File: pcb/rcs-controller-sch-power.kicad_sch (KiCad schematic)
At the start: 62 parts, among them J1 00222-32051, J10 0022-232021, J2 0022-232021, J3 0022-232041, J8 00222-32051, Q1 SI7465DP-T1-E3, U2 MP26123DR-LF-Z, U3 TPS63070

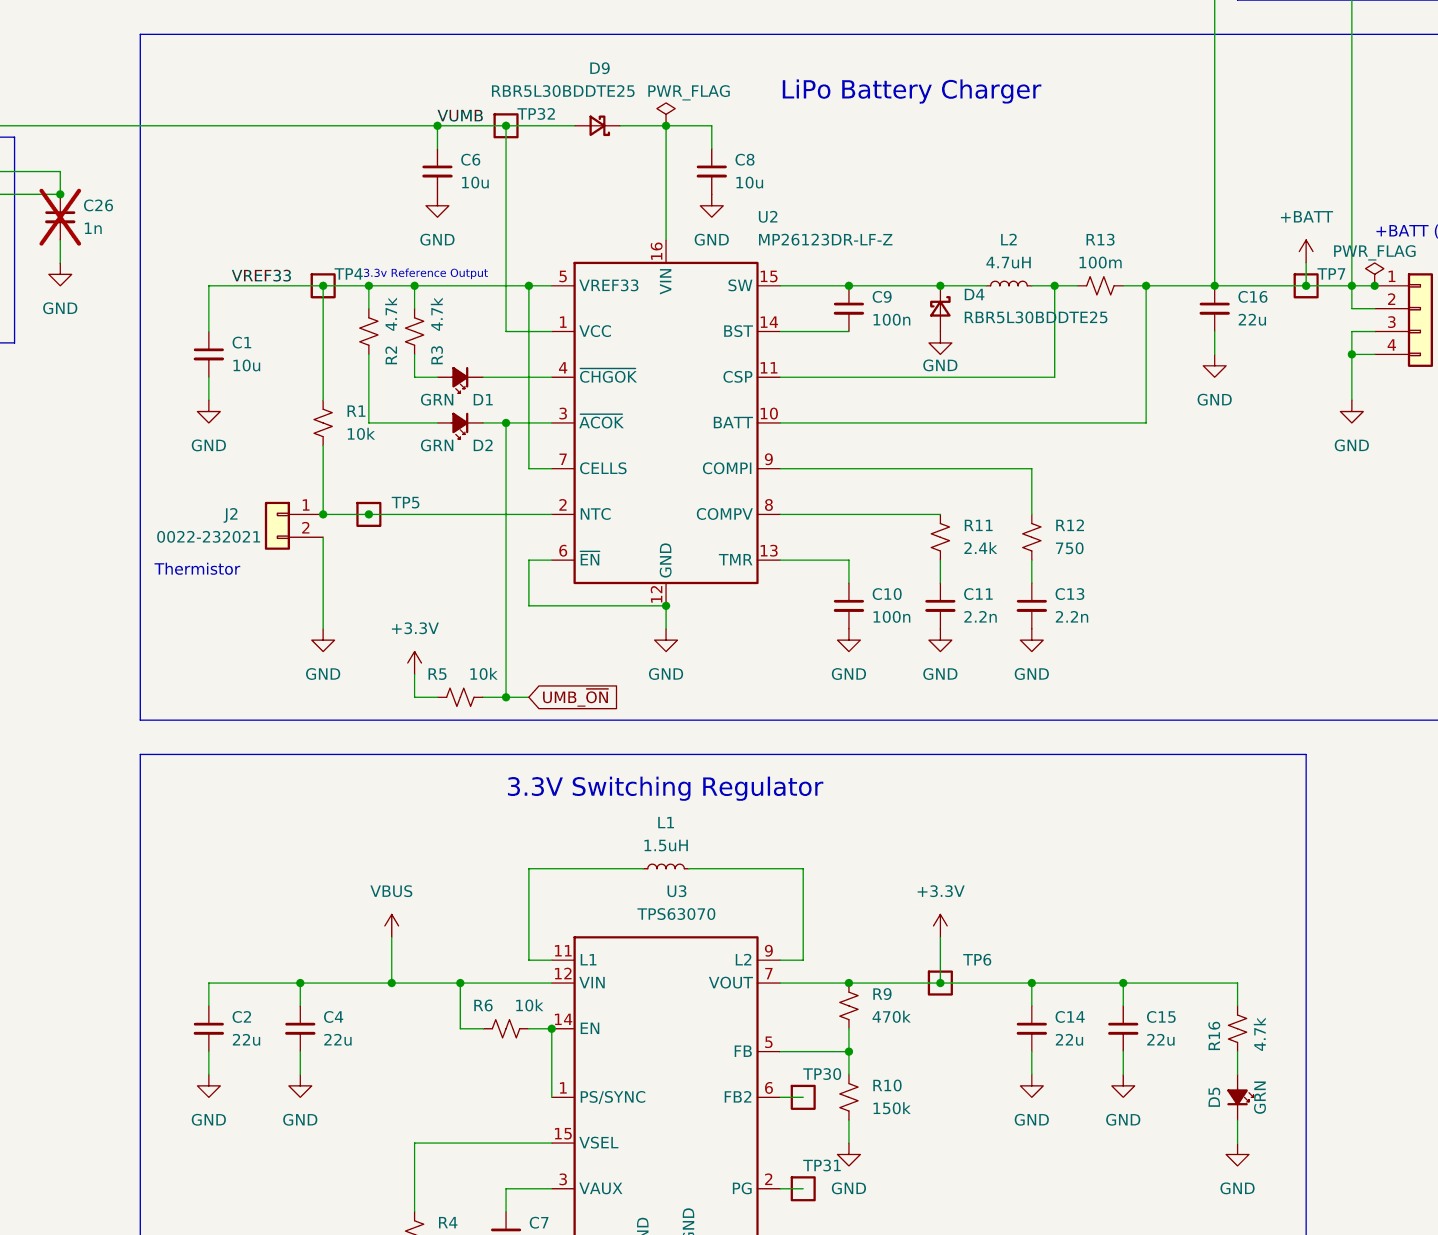
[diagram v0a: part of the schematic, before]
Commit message: power OR cleanup with Thomas for USB power
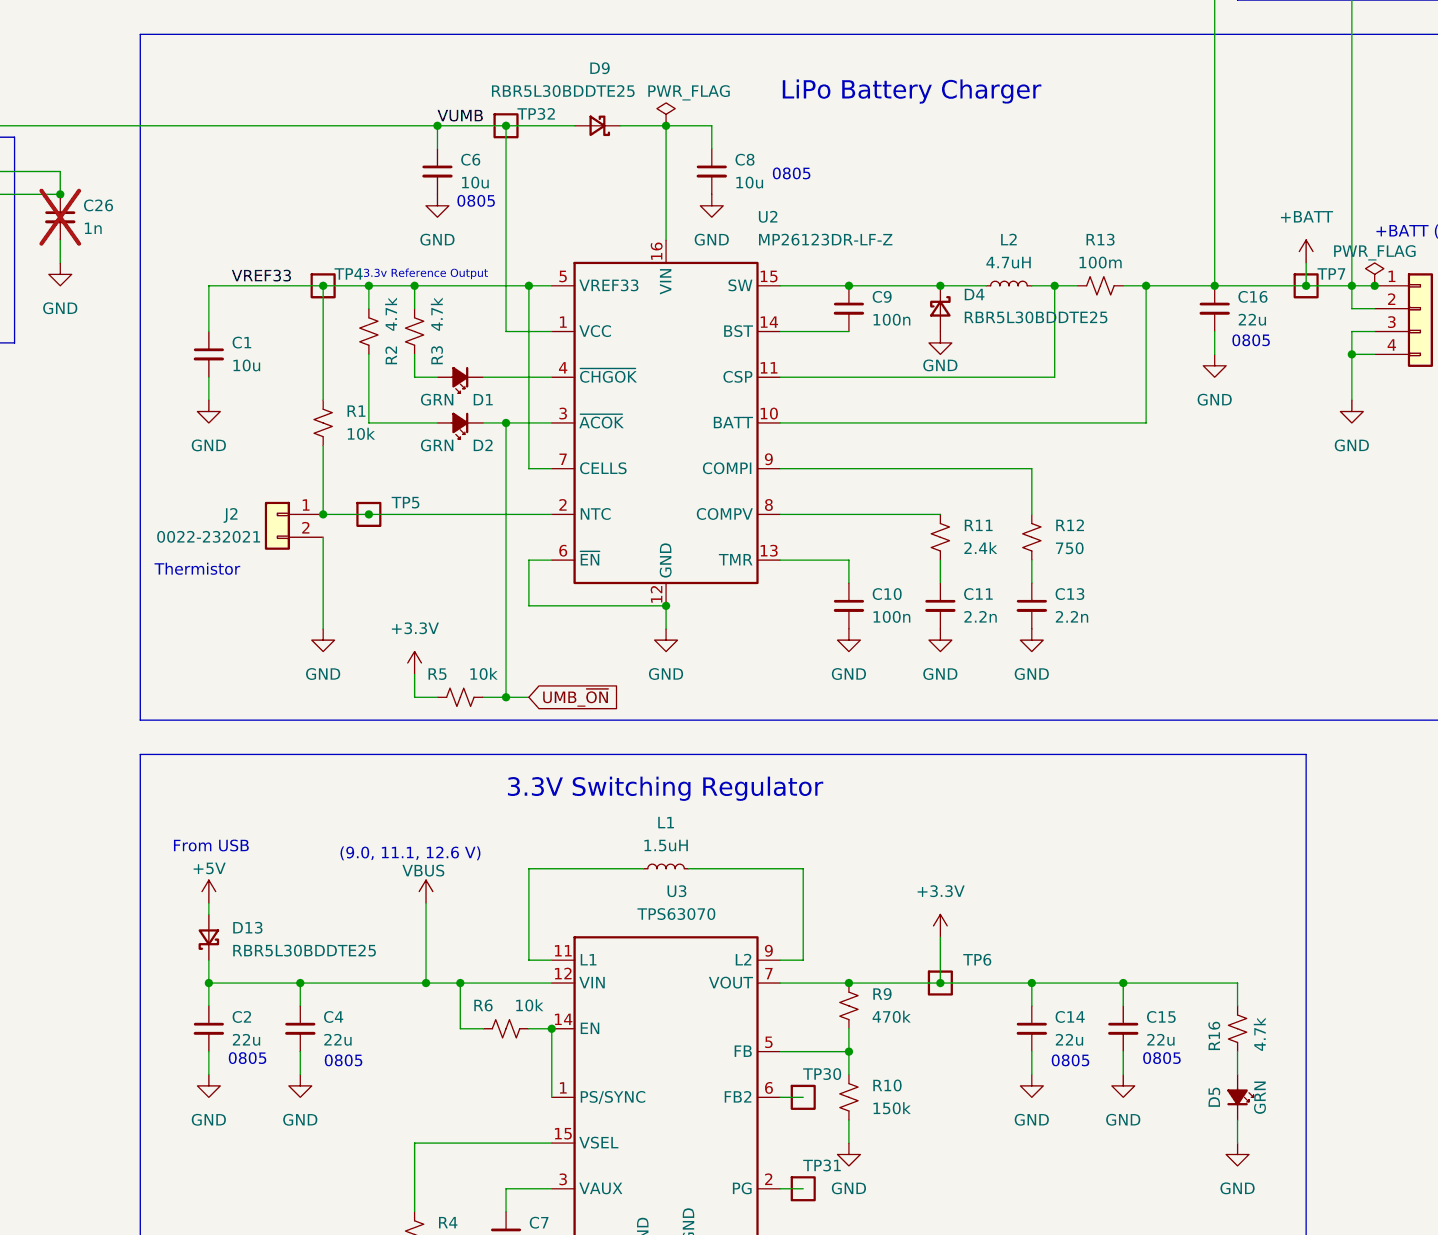
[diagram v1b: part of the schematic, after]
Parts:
- added D13: RBR5L30BDDTE25, Diode_SMD:D_SMA, symbol Device:D_Schottky_Small
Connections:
- net VBUS: now also D13.1 (K)
- new net +5V: D13.2 (A)
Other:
- note added: "(9.0, 11.1, 12.6 V)"
- note added: "0805"
- note added: "From USB"
